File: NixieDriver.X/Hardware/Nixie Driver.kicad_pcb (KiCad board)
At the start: 4 copper layers, 21.1 x 31.8 mm, 30 parts, among them J1 Conn_02x03_Odd_Even, J2 Conn_02x03_Odd_Even, J3 Conn_01x03, Q0 MMBTA42LT1G, Q1 MMBTA42LT1G, Q10 MMBTA42LT1G, Q2 MMBTA42LT1G, Q3 MMBTA42LT1G, Q4 MMBTA42LT1G, Q5 MMBTA42LT1G, Q6 MMBTA42LT1G, Q7 MMBTA42LT1G, Q8 MMBTA42LT1G, Q9 MMBTA42LT1G, U1 PIC16F15243

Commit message: STM32L011F4U MCU
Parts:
- removed J2: Conn_02x03_Odd_Even, Connector_PinHeader_2.54mm:PinHeader_1x04_P2.54mm_Vertical
- removed U1: PIC16F15243, Package_DFN_QFN:VQFN-20-1EP_3x3mm_P0.4mm_EP1.7x1.7mm
- added J4: Conn_01x03, Connector_PinHeader_2.54mm:PinHeader_1x02_P2.54mm_Vertical, B.Cu at (145.3, 94.2)
- added J5: Conn_01x03, Connector_PinHeader_2.54mm:PinHeader_1x02_P2.54mm_Vertical, B.Cu at (159.5, 94.2)
- added R13: 2.2k, Resistor_SMD:R_0603_1608Metric, F.Cu at (161.3, 93.7)
- added U2: STM32L011F4Ux, Package_DFN_QFN:ST_UFQFPN-20_3x3mm_P0.5mm, F.Cu at (152.4, 96.8)
- J1: value Conn_02x03_Odd_Even -> SWD; footprint Connector_PinHeader_2.54mm:PinHeader_1x03_P2.54mm_Vertical -> Connectory_PCB_Edge_:Tag-Connect EVC3-06; moved to F.Cu
- J3: footprint Connector_PinHeader_2.54mm:PinHeader_1x03_P2.54mm_Vertical -> Connector_PinHeader_2.54mm:PinHeader_1x02_P2.54mm_Vertical
- moved J3 10.8 mm to (153.4, 115.6), turned to 90 degrees
- moved C1 9.16 mm to (155.2, 95.8)
- moved Q6 6.81 mm to (152.4, 89.4), turned to -89.971 degrees
- moved R6 6.81 mm to (152.4, 89.4), turned to 90 degrees
- moved J1 6.81 mm to (141.9, 101.6), turned to 90 degrees
- moved Q3 5.88 mm to (148.8, 103.6), turned to 180 degrees
- moved R3 5.88 mm to (148.8, 103.6), turned to 0 degrees
- moved Q4 5.84 mm to (148.8, 99.1), turned to 180 degrees
- moved R4 5.84 mm to (148.8, 99.1), turned to 0 degrees
- moved Q0 5.17 mm to (160.0, 109.7), turned to 135 degrees
- moved Q2 5.17 mm to (144.8, 109.7), turned to 45 degrees
- moved R0 5.17 mm to (160.0, 109.7), turned to -45 degrees
- moved R2 5.17 mm to (144.8, 109.7), turned to -135 degrees
- moved R12 4.93 mm to (153.4, 112.8)
- moved R10 4.24 mm to (157.2, 113.0), turned to 0 degrees
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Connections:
- J1 pad 1: /~{MCLR} -> Vdd
- J1 pad 2: /SDA -> /SWDIO
- J1 pad 3: /SCL -> /NRST
- J3 pad 2: Vdd -> Vnn
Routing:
- net /ADDR3: track 23.4 -> 0.00 mm, vias 1 -> 0
- net /ADDR2: track 21.5 -> 0.00 mm, vias 1 -> 0
- net /ADDR1/CLK: track 19.9 -> 0.00 mm, vias 1 -> 0
- net /ADDR0/DAT: track 18.6 -> 0.00 mm, vias 1 -> 0
- net /SWDIO: track 0.00 -> 17.6 mm, vias 0 -> 1
- net Vdd: track 10.8 -> 28.2 mm, vias 1 -> 2
- net /ADDR: track 0.00 -> 14.7 mm, vias 0 -> 1
- net /SWCLK: track 0.00 -> 12.7 mm, vias 0 -> 1
- net /Driver_1: track 5.94 -> 18.5 mm
- net /NRST: track 0.00 -> 12.4 mm, vias 0 -> 1
- net /Driver_7: track 19.0 -> 6.68 mm
- net /Driver_Dot: track 5.98 -> 17.5 mm, vias 0 -> 2
- net /~{MCLR}: track 11.0 -> 0.00 mm, vias 1 -> 0
- net /Driver_4: track 13.6 -> 3.43 mm
- net /Driver_8: track 16.4 -> 6.30 mm
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- added copper zone on F.Cu, net GND
- added copper zone on In1.Cu, net GND
- added copper zone on In2.Cu, net GND
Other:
- board text added: "Nixie Driver V2 Aaron Johnson Oct. 2027"
- board text removed: "Nixie Driver V2 Aaron Johnson Feb. 2026"

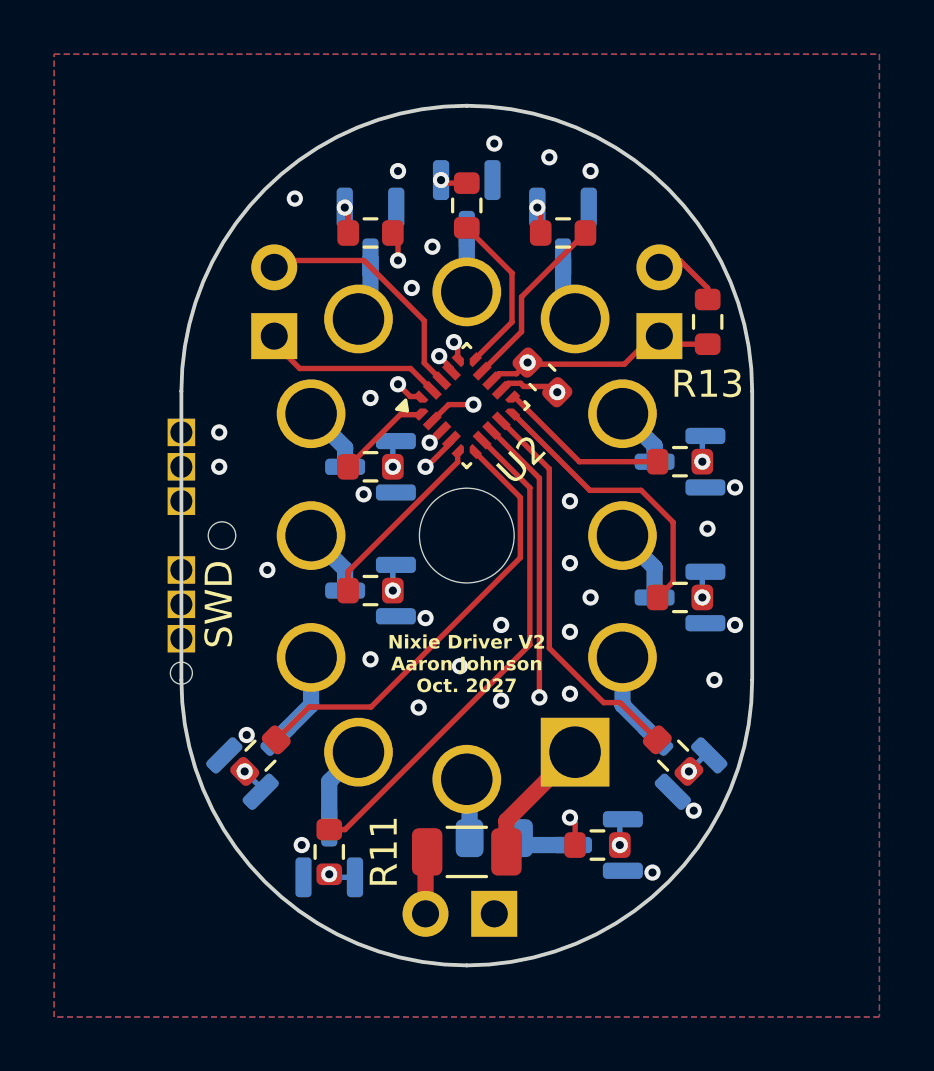
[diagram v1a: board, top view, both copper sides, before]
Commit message: improved ground plane continuity
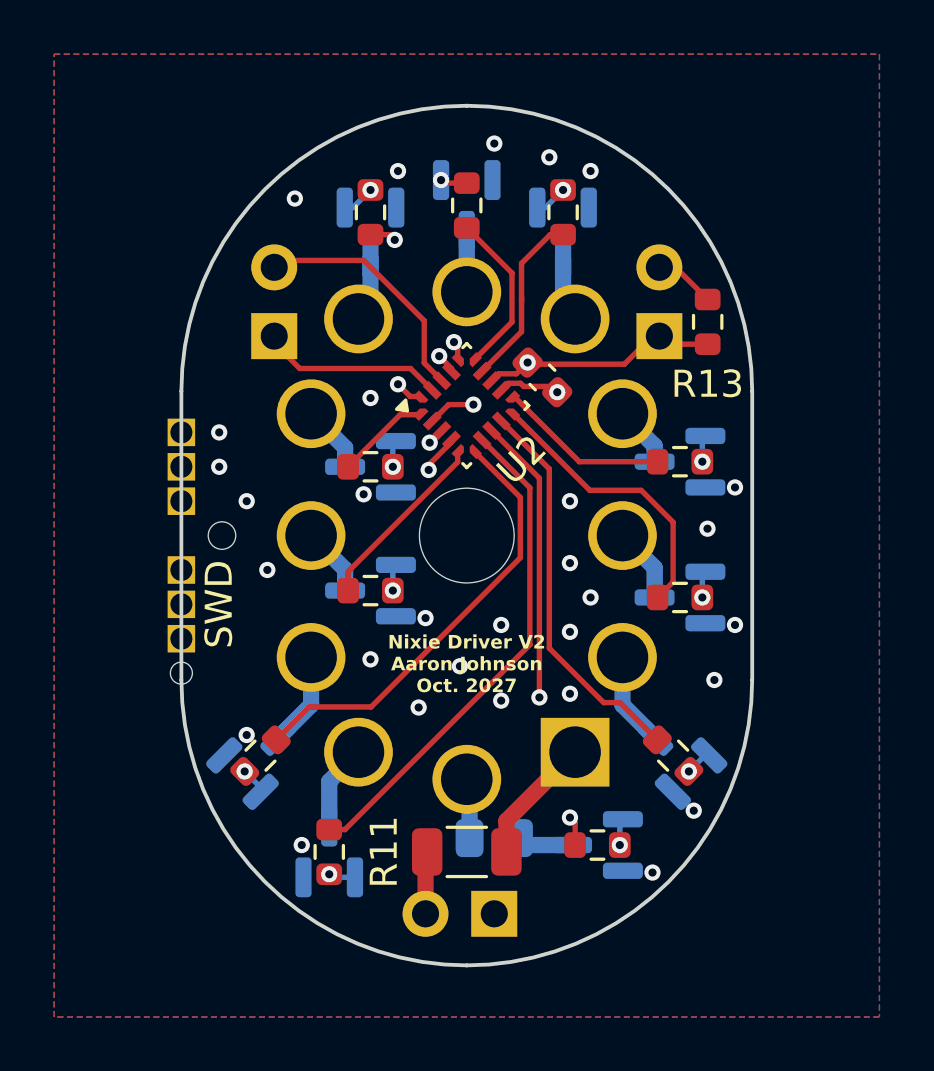
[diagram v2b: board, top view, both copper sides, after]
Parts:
- moved R5 0.76 mm to (148.8, 89.7), turned to 90 degrees
- moved R7 0.76 mm to (156.0, 89.7), turned to 90 degrees
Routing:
- net /SWDIO: track 17.6 -> 16.7 mm, vias 1 -> 2
- net /Driver_5: track 6.82 -> 7.57 mm
- net GND: vias 32 -> 30

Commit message: Switched to pin assignments that will actually work.
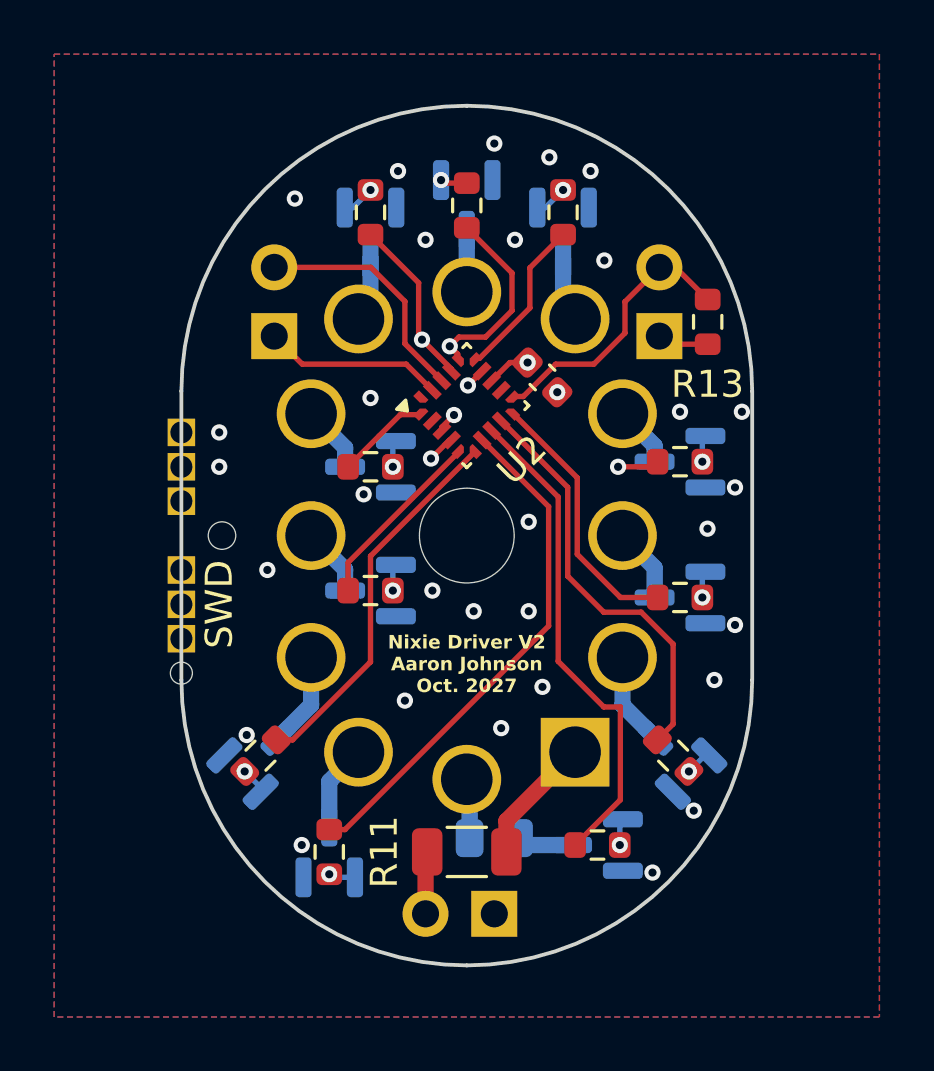
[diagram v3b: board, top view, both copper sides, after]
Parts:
- renumbered J5 to J2
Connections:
- J1 pad 2: /SWDIO -> /SWDIO/Driver_6
- J1 pad 4: /SWCLK -> /SWCLK/Driver_5
- R5 pad 1: /Driver_5 -> /SWCLK/Driver_5
- R6 pad 1: /Driver_6 -> /SWDIO/Driver_6
- U2 pad 11: /Driver_8 -> /ADDR
- U2 pad 14: /Driver_7 -> /Driver_8
- U2 pad 15: /Driver_6 -> /Driver_7
- U2 pad 16: /SWDIO -> /SWDIO/Driver_6
- U2 pad 17: /SWCLK -> /SWCLK/Driver_5
- U2 pad 2: /ADDR -> unconnected-(U2-PC15-Pad2)
- U2 pad 20: /Driver_5 -> unconnected-(U2-PB9-Pad20)
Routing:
- net /SWDIO/Driver_6: track 0.00 -> 24.6 mm, vias 0 -> 1
- net /SWCLK/Driver_5: track 0.00 -> 18.2 mm, vias 0 -> 1
- net /SWDIO: track 16.7 -> 0.00 mm, vias 2 -> 0
- net /SWCLK: track 12.7 -> 0.00 mm, vias 1 -> 0
- net /Driver_5: track 7.57 -> 0.00 mm, vias 2 -> 0
- net Vdd: track 28.5 -> 22.2 mm
- net /Driver_6: track 6.06 -> 0.00 mm
- net /ADDR: track 14.5 -> 10.5 mm, vias 1 -> 0
- net /Driver_8: track 6.30 -> 9.07 mm, vias 0 -> 2
- net GND: track 2.48 -> 0.00 mm, vias 30 -> 31
- net /Driver_2: track 16.3 -> 14.0 mm
- net /NRST: track 12.4 -> 13.6 mm
- net /Driver_0: track 14.5 -> 15.5 mm
- net /Driver_Dot: track 17.5 -> 18.3 mm, vias 2 -> 0
- net /Driver_9: track 10.5 -> 9.75 mm
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
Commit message: Fixed  pin socket 3d model path
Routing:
- net Vdd: track 22.2 -> 27.7 mm
- net GND: track 0.00 -> 2.31 mm
- net /ADDR: track 10.5 -> 11.7 mm, vias 0 -> 1
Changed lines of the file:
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@@
 		)
 		(embedded_fonts no)
-		(model "${KICAD_MY_3D}/0373-0-15-80-34-80-10-0.step"
+		(model "${REPO}/3d/0373-0-15-80-34-80-10-0.step"
 			(offset
 				(xyz 0 9 0)
@@
 			)
 			(rotate
-				(xyz 0 0 0)
+				(xyz -0 -0 -0)
 			)
 		)
-		(model "${KICAD_MY_3D}/0373-0-15-80-34-80-10-0.step"
+		(model "${REPO}/3d/0373-0-15-80-34-80-10-0.step"
 			(offset
 				(xyz 0 -9 0)
@@
 			)
 		)
-		(model "${KICAD_MY_3D}/0373-0-15-80-34-80-10-0.step"
+		(model "${REPO}/3d/0373-0-15-80-34-80-10-0.step"
 			(offset
 				(xyz 4 8 0)
@@
 			)
 		)
-		(model "${KICAD_MY_3D}/0373-0-15-80-34-80-10-0.step"
+		(model "${REPO}/3d/0373-0-15-80-34-80-10-0.step"
 			(offset
 				(xyz -4 8 0)
@@
 			)
 		)
-		(model "${KICAD_MY_3D}/0373-0-15-80-34-80-10-0.step"
+		(model "${REPO}/3d/0373-0-15-80-34-80-10-0.step"
 			(offset
 				(xyz 4 -8 0)
@@
 			)
 		)
-		(model "${KICAD_MY_3D}/0373-0-15-80-34-80-10-0.step"
+		(model "${REPO}/3d/0373-0-15-80-34-80-10-0.step"
 			(offset
 				(xyz -4 -8 0)
@@
 			)
 		)
-		(model "${KICAD_MY_3D}/0373-0-15-80-34-80-10-0.step"
+		(model "${REPO}/3d/0373-0-15-80-34-80-10-0.step"
 			(offset
 				(xyz 5.75 4.5 0)
@@
 			)
 		)
-		(model "${KICAD_MY_3D}/0373-0-15-80-34-80-10-0.step"
+		(model "${REPO}/3d/0373-0-15-80-34-80-10-0.step"
 			(offset
 				(xyz 5.75 -4.5 0)
@@
 			)
 		)
-		(model "${KICAD_MY_3D}/0373-0-15-80-34-80-10-0.step"
+		(model "${REPO}/3d/0373-0-15-80-34-80-10-0.step"
 			(offset
 				(xyz 5.75 0 0)
@@
 			)
 		)
-		(model "${KICAD_MY_3D}/0373-0-15-80-34-80-10-0.step"
+		(model "${REPO}/3d/0373-0-15-80-34-80-10-0.step"
 			(offset
 				(xyz -5.75 -4.5 0)
@@
 			)
 		)
-		(model "${KICAD_MY_3D}/0373-0-15-80-34-80-10-0.step"
+		(model "${REPO}/3d/0373-0-15-80-34-80-10-0.step"
 			(offset
 				(xyz -5.75 0 0)
@@
 			)
 		)
-		(model "${KICAD_MY_3D}/0373-0-15-80-34-80-10-0.step"
+		(model "${REPO}/3d/0373-0-15-80-34-80-10-0.step"
 			(offset
 				(xyz -5.75 4.5 0)
@@
 	)
 	(segment
+		(start 157.192 95.504)
+		(end 154.94 95.504)
+		(width 0.2)
+		(layer "In1.Cu")
+		(net "Vdd")
+	)
+	(segment
+		(start 158.462 94.234)
+		(end 157.192 95.504)
+		(width 0.2)
+		(layer "In1.Cu")
+		(net "Vdd")
+	)
+	(segment
+		(start 154.94 95.504)
+		(end 154.645992 95.209992)
+		(width 0.2)
+		(layer "In1.Cu")
+		(net "Vdd")
+	)
+	(segment
+		(start 159.512 94.234)
+		(end 158.462 94.234)
+		(width 0.2)
+		(layer "In1.Cu")
+		(net "Vdd")
+	)
+	(segment
 		(start 146.776 104.43)
 		(end 142.999 104.43)
@@
 		(net "/NRST")
 	)
+	(segment
+		(start 153.930193 95.976914)
+		(end 154.384216 95.976914)
+		(width 0.2)
+		(layer "F.Cu")
+		(net "GND")
+	)
+	(segment
+		(start 154.71331 96.306008)
+		(end 155.742008 96.306008)
+		(width 0.2)
+		(layer "F.Cu")
+		(net "GND")
+	)
+	(segment
+		(start 153.672792 96.234315)
+		(end 153.930193 95.976914)
+		(width 0.2)
+		(layer "F.Cu")
+		(net "GND")
+	)
+	(segment
+		(start 154.384216 95.976914)
+		(end 154.71331 96.306008)
+		(width 0.2)
+		(layer "F.Cu")
+		(net "GND")
+	)
 	(via
 		(at 155.194 107.188)
@@
 	)
 	(segment
+		(start 154.259549 96.464124)
+		(end 155.008712 97.213287)
+		(width 0.2)
+		(layer "F.Cu")
+		(net "/ADDR")
+	)
+	(segment
 		(start 159.766 91.44)
 		(end 159.855 91.44)
@@
 	(segment
 		(start 154.150089 96.464124)
-		(end 154.487876 96.464124)
+		(end 154.259549 96.464124)
 		(width 0.2)
 		(layer "F.Cu")
@@
 	)
 	(segment
-		(start 157.091737 95.27)
-		(end 158.242 94.119737)
+		(start 159.512 91.694)
+		(end 159.766 91.44)
 		(width 0.2)
 		(layer "F.Cu")
@@
 	)
 	(segment
-		(start 158.242 94.119737)
-		(end 158.242 92.964)
+		(start 159.855 91.44)
+		(end 161.297 92.882)
 		(width 0.2)
 		(layer "F.Cu")
 		(net "/ADDR")
 	)
+	(via
+		(at 155.008712 97.213287)
+		(size 0.6)
+		(drill 0.3)
+		(layers "F.Cu" "B.Cu")
+		(net "/ADDR")
+	)
 	(segment
-		(start 154.487876 96.464124)
-		(end 155.682 95.27)
+		(start 155.996804 95.27)
+		(end 157.091737 95.27)
 		(width 0.2)
-		(layer "F.Cu")
+		(layer "In2.Cu")
 		(net "/ADDR")
 	)
 	(segment
-		(start 159.512 91.694)
-		(end 159.766 91.44)
+		(start 155.008712 96.258092)
+		(end 155.996804 95.27)
 		(width 0.2)
-		(layer "F.Cu")
+		(layer "In2.Cu")
 		(net "/ADDR")
 	)
 	(segment
-		(start 159.855 91.44)
-		(end 161.297 92.882)
+		(start 155.008712 97.213287)
+		(end 155.008712 96.258092)
 		(width 0.2)
-		(layer "F.Cu")
+		(layer "In2.Cu")
 		(net "/ADDR")
 	)
 	(segment
-		(start 155.682 95.27)
-		(end 157.091737 95.27)
+		(start 157.091737 95.27)
+		(end 158.4096 93.952137)
 		(width 0.2)
-		(layer "F.Cu")
+		(layer "In2.Cu")
+		(net "/ADDR")
+	)
+	(segment
+		(start 158.4096 93.952137)
+		(end 158.4096 92.7964)
+		(width 0.2)
+		(layer "In2.Cu")
 		(net "/ADDR")
 	)
 	(segment
-		(start 158.242 92.964)
+		(start 158.4096 92.7964)
 		(end 159.512 91.694)
 		(width 0.2)
-		(layer "F.Cu")
+		(layer "In2.Cu")
 		(net "/ADDR")
 	)

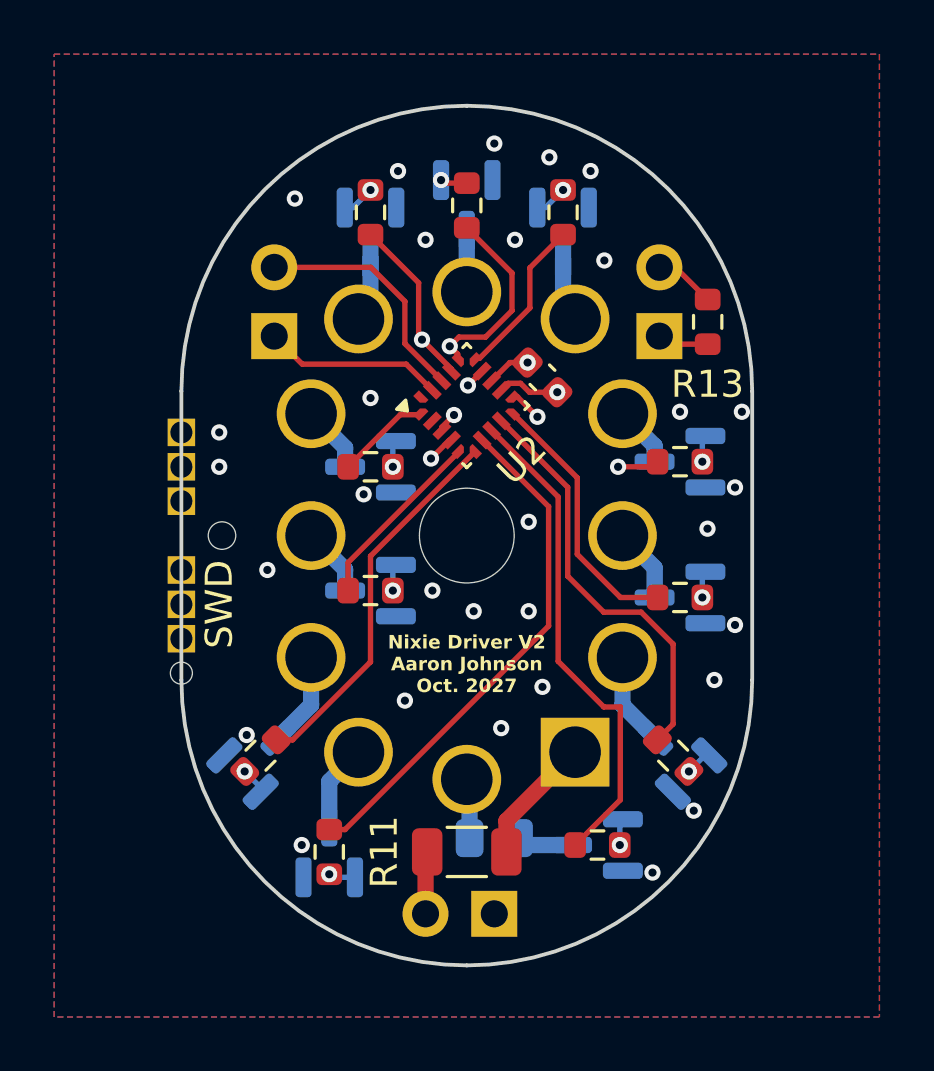
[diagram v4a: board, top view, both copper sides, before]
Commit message: Flipped edge connector so it doesn't hit pin sockets
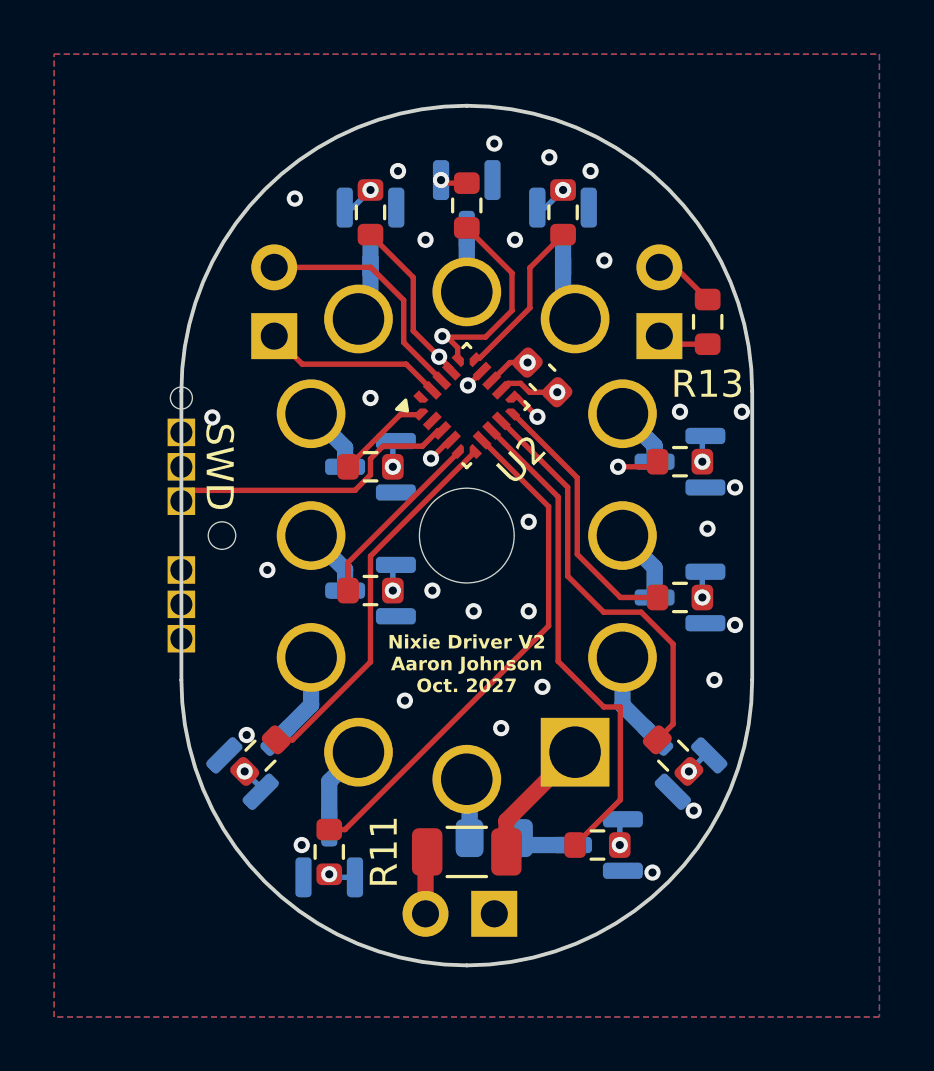
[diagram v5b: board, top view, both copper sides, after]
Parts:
- J1: moved to B.Cu
- turned J1 to -90 degrees
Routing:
- net /SWDIO/Driver_6: track 24.6 -> 19.8 mm, vias 1 -> 2
- net /SWCLK/Driver_5: track 18.2 -> 22.2 mm
- net Vdd: track 27.7 -> 25.0 mm
- net /NRST: track 13.6 -> 11.0 mm, vias 1 -> 0
- net GND: vias 31 -> 28
